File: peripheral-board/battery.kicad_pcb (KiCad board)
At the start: 2 copper layers, 50 x 10 mm, 20 parts, among them J1001 CONN_01X03, Q5001 IRLML2244TRPbF, Q5002 IRLML2244TRPbF, U5002 TL431, U5003 TL431

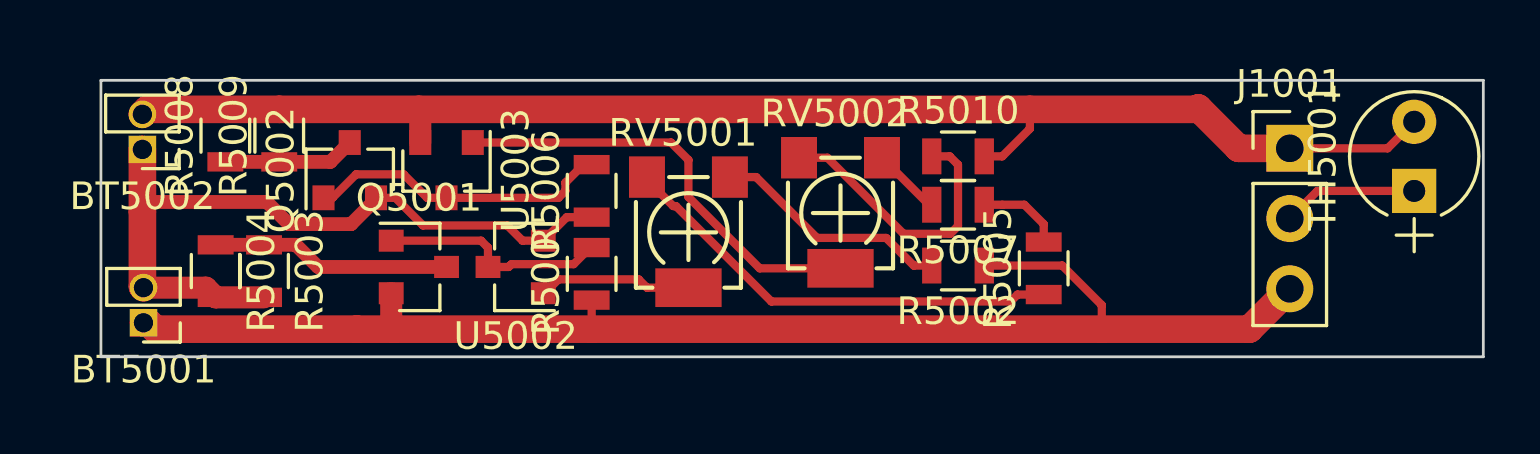
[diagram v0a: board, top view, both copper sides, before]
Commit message: fixed faulty schematic in battery balancer
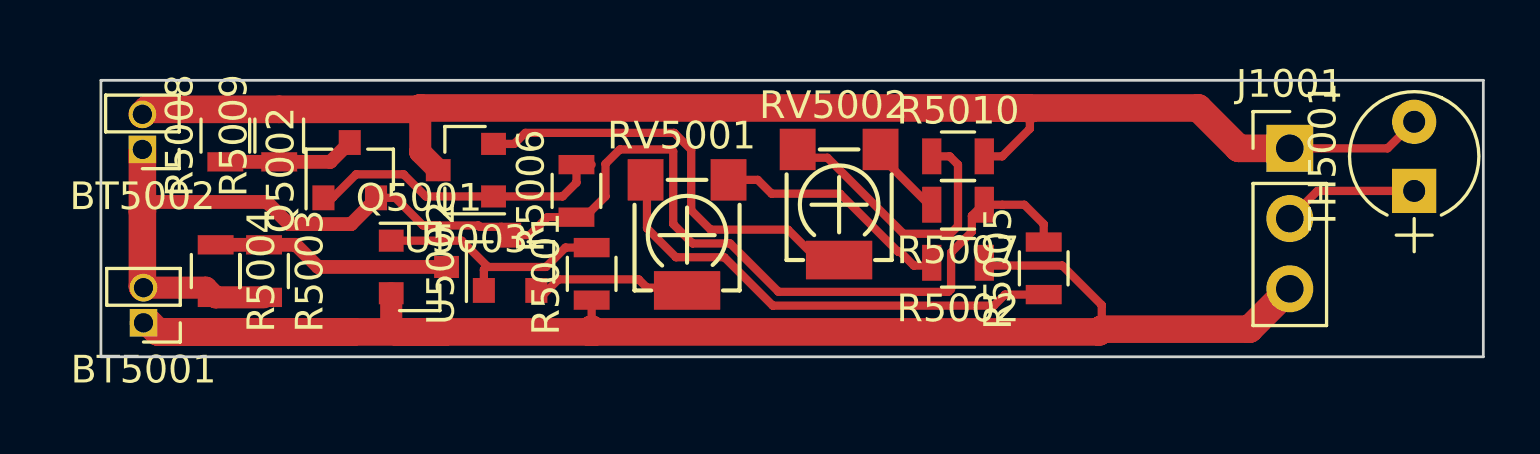
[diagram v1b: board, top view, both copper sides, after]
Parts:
- moved U5003 0.70 mm to (133.2, 113.2), turned to 180 degrees
- moved R5006 0.55 mm to (137.2, 114.0)
- moved RV5002 0.30 mm to (146.7, 114.5)
- moved U5002 0.25 mm to (134.8, 116.6), turned to 90 degrees
- moved RV5001 0.11 mm to (141.2, 115.6)
- moved R5002 0.10 mm to (151.0, 116.6)
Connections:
- R5005 pad 2: Net-(R5005-Pad2) -> Net-(BT5001-Pad2)
- R5007 pad 1: Net-(R5005-Pad2) -> Net-(BT5001-Pad2)
- U5002 pad 1: Net-(RV5001-Pad2) -> Net-(Q5001-Pad1)
- U5002 pad 2: Net-(BT5001-Pad2) -> Net-(RV5001-Pad2)
- U5002 pad 3: Net-(Q5001-Pad1) -> Net-(BT5001-Pad2)
- U5003 pad 1: Net-(RV5002-Pad2) -> Net-(Q5002-Pad1)
- U5003 pad 2: /B- -> Net-(RV5002-Pad2)
- U5003 pad 3: Net-(Q5002-Pad1) -> /B-
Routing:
- net Net-(BT5001-Pad2): track 27.7 -> 52.6 mm
- net /B+: track 52.6 -> 61.7 mm
- net Net-(R5005-Pad2): track 3.09 -> 0.00 mm
- net /B-: track 51.1 -> 54.1 mm
- net Net-(R5005-Pad1): track 16.4 -> 17.5 mm
- net Net-(Q5001-Pad1): track 8.34 -> 8.87 mm
